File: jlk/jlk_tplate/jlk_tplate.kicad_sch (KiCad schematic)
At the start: 38 parts, among them SW0 SWITCH_PUSH, SW1 SWITCH_PUSH, SW10 SWITCH_PUSH, SW11 SWITCH_PUSH, SW12 SWITCH_PUSH, SW13 SWITCH_PUSH, SW14 SWITCH_PUSH, SW15 SWITCH_PUSH, SW16 SWITCH_PUSH, SW17 SWITCH_PUSH, SW18 SWITCH_PUSH, SW19 SWITCH_PUSH, SW2 SWITCH_PUSH, SW20 SWITCH_PUSH, SW21 SWITCH_PUSH, SW22 SWITCH_PUSH, SW23 SWITCH_PUSH, SW24 SWITCH_PUSH, SW25 SWITCH_PUSH, SW26 SWITCH_PUSH, SW27 SWITCH_PUSH, SW28 SWITCH_PUSH, SW29 SWITCH_PUSH, SW3 SWITCH_PUSH, SW30 SWITCH_PUSH, SW31 SWITCH_PUSH, SW32 SWITCH_PUSH, SW33 SWITCH_PUSH, SW4 SWITCH_PUSH, SW5 SWITCH_PUSH, SW6 SWITCH_PUSH, SW7 SWITCH_PUSH, SW8 SWITCH_PUSH, SW9 SWITCH_PUSH

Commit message: Switched to SMD diode, col2row.
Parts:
- removed H12, H13, H14, H15: MountingHole, MountingHole:MountingHole_2.2mm_M2_ISO7380_Pad, symbol Mechanical:MountingHole
- added H0, H1, H10, H11, H2, H3, H4, H5, H6, H7, H8, H9: MountingHole, MountingHole:MountingHole_2.2mm_M2_ISO7380_Pad, symbol Mechanical:MountingHole
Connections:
- net COL1: now also SW0.1, SW1.1, SW2.1; no longer SW0.3 (K), SW1.3 (K), SW2.3 (K)
- net COL10: now also SW31.1, SW32.1, SW33.1; no longer SW31.3 (K), SW32.3 (K), SW33.3 (K)
- net COL2: now also SW3.1, SW4.1, SW5.1; no longer SW3.3 (K), SW4.3 (K), SW5.3 (K)
- net COL3: now also SW6.1, SW7.1, SW8.1; no longer SW6.3 (K), SW7.3 (K), SW8.3 (K)
- net COL4: now also SW10.1, SW11.1, SW12.1, SW9.1; no longer SW10.3 (K), SW11.3 (K), SW12.3 (K), SW9.3 (K)
- net COL5: now also SW13.1, SW14.1, SW15.1, SW16.1; no longer SW13.3 (K), SW14.3 (K), SW15.3 (K), SW16.3 (K)
- net COL6: now also SW17.1, SW18.1, SW19.1, SW20.1; no longer SW17.3 (K), SW18.3 (K), SW19.3 (K), SW20.3 (K)
- net COL7: now also SW21.1, SW22.1, SW23.1, SW24.1; no longer SW21.3 (K), SW22.3 (K), SW23.3 (K), SW24.3 (K)
- net COL8: now also SW25.1, SW26.1, SW27.1; no longer SW25.3 (K), SW26.3 (K), SW27.3 (K)
- net COL9: now also SW28.1, SW29.1, SW30.1; no longer SW28.3 (K), SW29.3 (K), SW30.3 (K)
- net ROW0: now also SW12.3 (K), SW16.3 (K), SW20.3 (K), SW24.3 (K); no longer SW12.1, SW16.1, SW20.1, SW24.1
- net ROW1: now also SW11.3 (K), SW15.3 (K), SW19.3 (K), SW2.3 (K), SW23.3 (K), SW27.3 (K), SW30.3 (K), SW33.3 (K), SW5.3 (K), SW8.3 (K); no longer SW11.1, SW15.1, SW19.1, SW2.1, SW23.1, SW27.1, SW30.1, SW33.1, SW5.1, SW8.1
- net ROW2: now also SW1.3 (K), SW10.3 (K), SW14.3 (K), SW18.3 (K), SW22.3 (K), SW26.3 (K), SW29.3 (K), SW32.3 (K), SW4.3 (K), SW7.3 (K); no longer SW1.1, SW10.1, SW14.1, SW18.1, SW22.1, SW26.1, SW29.1, SW32.1, SW4.1, SW7.1
- net ROW3: now also SW0.3 (K), SW13.3 (K), SW17.3 (K), SW21.3 (K), SW25.3 (K), SW28.3 (K), SW3.3 (K), SW31.3 (K), SW6.3 (K), SW9.3 (K); no longer SW0.1, SW13.1, SW17.1, SW21.1, SW25.1, SW28.1, SW3.1, SW31.1, SW6.1, SW9.1

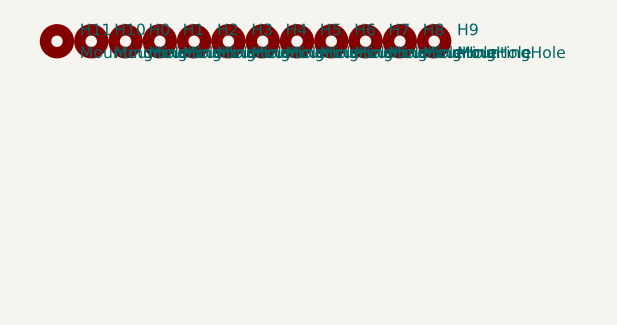
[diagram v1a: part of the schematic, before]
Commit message: Changed jlk for mounting promicro under the pcb.
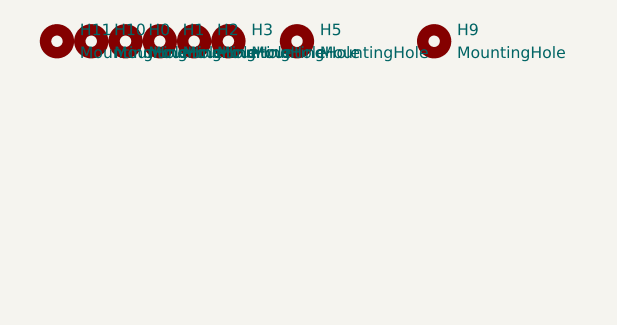
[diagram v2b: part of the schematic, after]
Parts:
- removed H4, H6, H7, H8: MountingHole, MountingHole:MountingHole_2.2mm_M2_ISO7380_Pad, symbol Mechanical:MountingHole
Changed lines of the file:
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@@
-    )
-  )
-  (symbol (lib_id "Mechanical:MountingHole") (at 387.35 33.02 0) (unit 1)
-    (in_bom yes) (on_board yes) (dnp no) (fields_autoplaced)
-    (property "Reference" "H8" (at 389.89 31.75 0)
-      (effects (font (size 1.27 1.27)) (justify left))
-    )
-    (property "Value" "MountingHole" (at 389.89 34.29 0)
-      (effects (font (size 1.27 1.27)) (justify left))
-    )
-    (property "Footprint" "MountingHole:MountingHole_2.2mm_M2_ISO7380_Pad" (at 387.35 33.02 0)
-      (effects (font (size 1.27 1.27)) hide)
-    )
-    (property "Datasheet" "~" (at 387.35 33.02 0)
-      (effects (font (size 1.27 1.27)) hide)
-    )
-    (instances
-      (project "jlk_tplate"
-        (path "/97127b28-60f4-45ff-835e-dccfbc833331"
-          (reference "H8") (unit 1)
-        )
-      )
     )
   )
@@
     )
   )
-  (symbol (lib_id "Mechanical:MountingHole") (at 379.73 33.02 0) (unit 1)
-    (in_bom yes) (on_board yes) (dnp no) (fields_autoplaced)
-    (property "Reference" "H6" (at 382.27 31.75 0)
-      (effects (font (size 1.27 1.27)) (justify left))
-    )
-    (property "Value" "MountingHole" (at 382.27 34.29 0)
-      (effects (font (size 1.27 1.27)) (justify left))
-    )
-    (property "Footprint" "MountingHole:MountingHole_2.2mm_M2_ISO7380_Pad" (at 379.73 33.02 0)
-      (effects (font (size 1.27 1.27)) hide)
-    )
-    (property "Datasheet" "~" (at 379.73 33.02 0)
-      (effects (font (size 1.27 1.27)) hide)
-    )
-    (instances
-      (project "jlk_tplate"
-        (path "/97127b28-60f4-45ff-835e-dccfbc833331"
-          (reference "H6") (unit 1)
-        )
-      )
-    )
-  )
   (symbol (lib_id "Mechanical:MountingHole") (at 364.49 33.02 0) (unit 1)
     (in_bom yes) (on_board yes) (dnp no) (fields_autoplaced)
@@
         (path "/97127b28-60f4-45ff-835e-dccfbc833331"
           (reference "H2") (unit 1)
-        )
-      )
-    )
-  )
-  (symbol (lib_id "Mechanical:MountingHole") (at 372.11 33.02 0) (unit 1)
-    (in_bom yes) (on_board yes) (dnp no) (fields_autoplaced)
-    (property "Reference" "H4" (at 374.65 31.75 0)
-      (effects (font (size 1.27 1.27)) (justify left))
-    )
-    (property "Value" "MountingHole" (at 374.65 34.29 0)
-      (effects (font (size 1.27 1.27)) (justify left))
-    )
-    (property "Footprint" "MountingHole:MountingHole_2.2mm_M2_ISO7380_Pad" (at 372.11 33.02 0)
-      (effects (font (size 1.27 1.27)) hide)
-    )
-    (property "Datasheet" "~" (at 372.11 33.02 0)
-      (effects (font (size 1.27 1.27)) hide)
-    )
-    (instances
-      (project "jlk_tplate"
-        (path "/97127b28-60f4-45ff-835e-dccfbc833331"
-          (reference "H4") (unit 1)
         )
       )
@@
         )
       )
-    )
-  )
-  (symbol (lib_id "Mechanical:MountingHole") (at 383.54 33.02 0) (unit 1)
-    (in_bom yes) (on_board yes) (dnp no) (fields_autoplaced)
-    (property "Reference" "H7" (at 386.08 31.75 0)
-      (effects (font (size 1.27 1.27)) (justify left))
-    )
-    (property "Value" "MountingHole" (at 386.08 34.29 0)
-      (effects (font (size 1.27 1.27)) (justify left))
-    )
-    (property "Footprint" "MountingHole:MountingHole_2.2mm_M2_ISO7380_Pad" (at 383.54 33.02 0)
-      (effects (font (size 1.27 1.27)) hide)
-    )
-    (property "Datasheet" "~" (at 383.54 33.02 0)
-      (effects (font (size 1.27 1.27)) hide)
-    )
-    (instances
-      (project "jlk_tplate"
-        (path "/97127b28-60f4-45ff-835e-dccfbc833331"
-          (reference "H7") (unit 1)
-        )
-      )
